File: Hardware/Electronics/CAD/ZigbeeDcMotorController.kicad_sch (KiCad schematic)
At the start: 13 parts, among them J1 Conn_01x02, J3 Conn_01x02, J4 Conn_01x04, J5 Conn_01x07, K1 AZ832P2-x, Q1 BC846, Q3 BC846

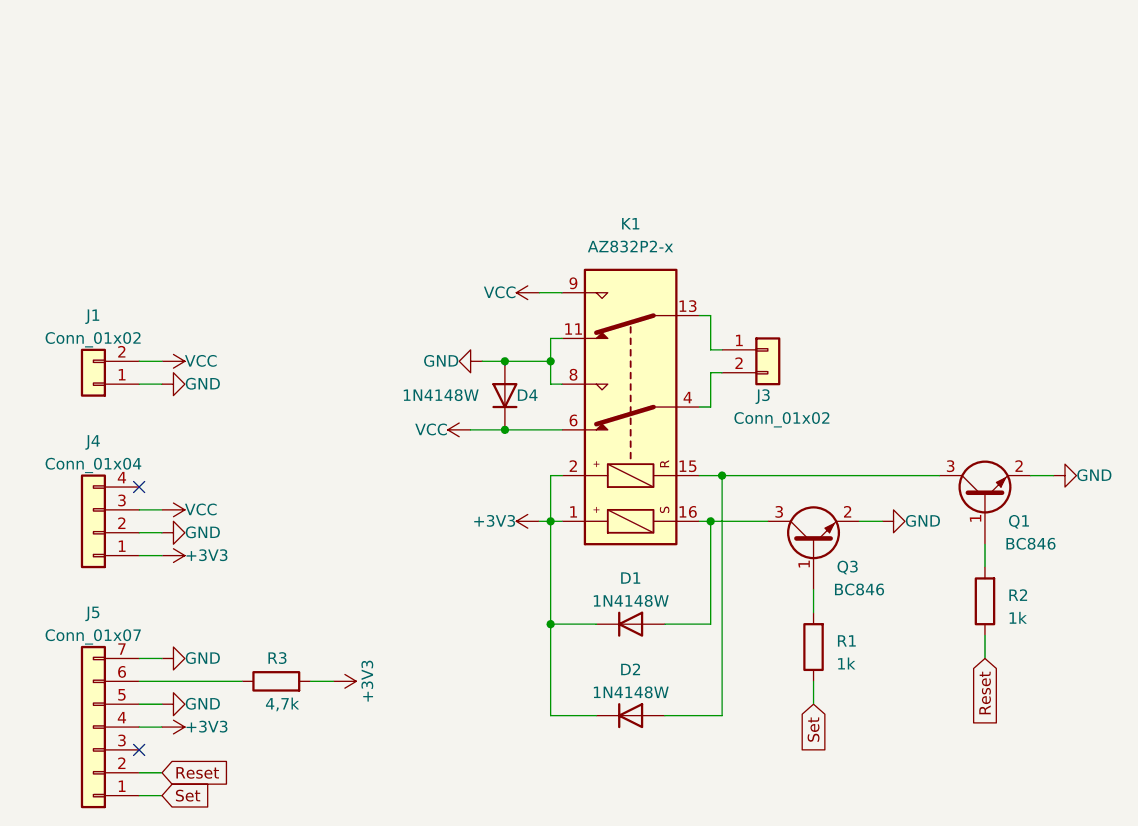
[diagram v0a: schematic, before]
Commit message: Second design with LDO
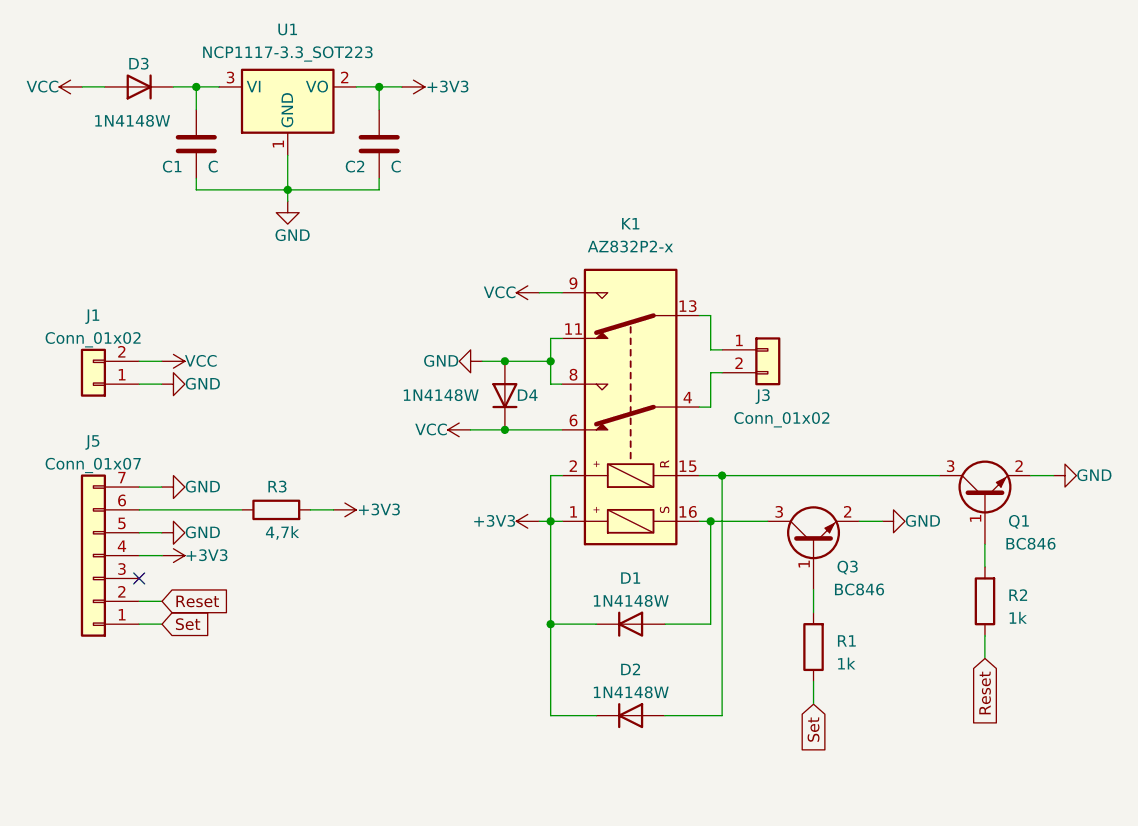
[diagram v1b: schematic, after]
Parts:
- removed J4: Conn_01x04, Connector_PinHeader_2.54mm:PinHeader_1x04_P2.54mm_Vertical, symbol Connector_Generic:Conn_01x04
- added C1, C2: C, Capacitor_SMD:C_0805_2012Metric_Pad1.18x1.45mm_HandSolder, symbol Device:C
- added D3: 1N4148W, Diode_SMD:D_SOD-123, symbol Diode:1N4148W
- added U1: NCP1117-3.3_SOT223, Package_TO_SOT_SMD:SOT-223-3_TabPin2, symbol Regulator_Linear:NCP1117-3.3_SOT223
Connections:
- net +3V3: now also C2.1, U1.2 (VO)
- net GND: now also C1.2, C2.2, U1.1 (GND)
- net VCC: now also D3.2 (A)
- new net: C1.1, D3.1 (K), U1.3 (VI)
- no-connect marks 2 -> 1
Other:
- moved on the sheet: J5, R3
